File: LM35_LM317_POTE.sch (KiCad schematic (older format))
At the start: 21 parts, among them J10 TB_1X2, J6 TB_1X2, J7 TB_1X2, J8 TB_1X2, J9 TB_1X2, P10 CONN_01X02, P5 CONN_02X02, P6 CONN_01X02, P7 CONN_01X02, P8 CONN_01X02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

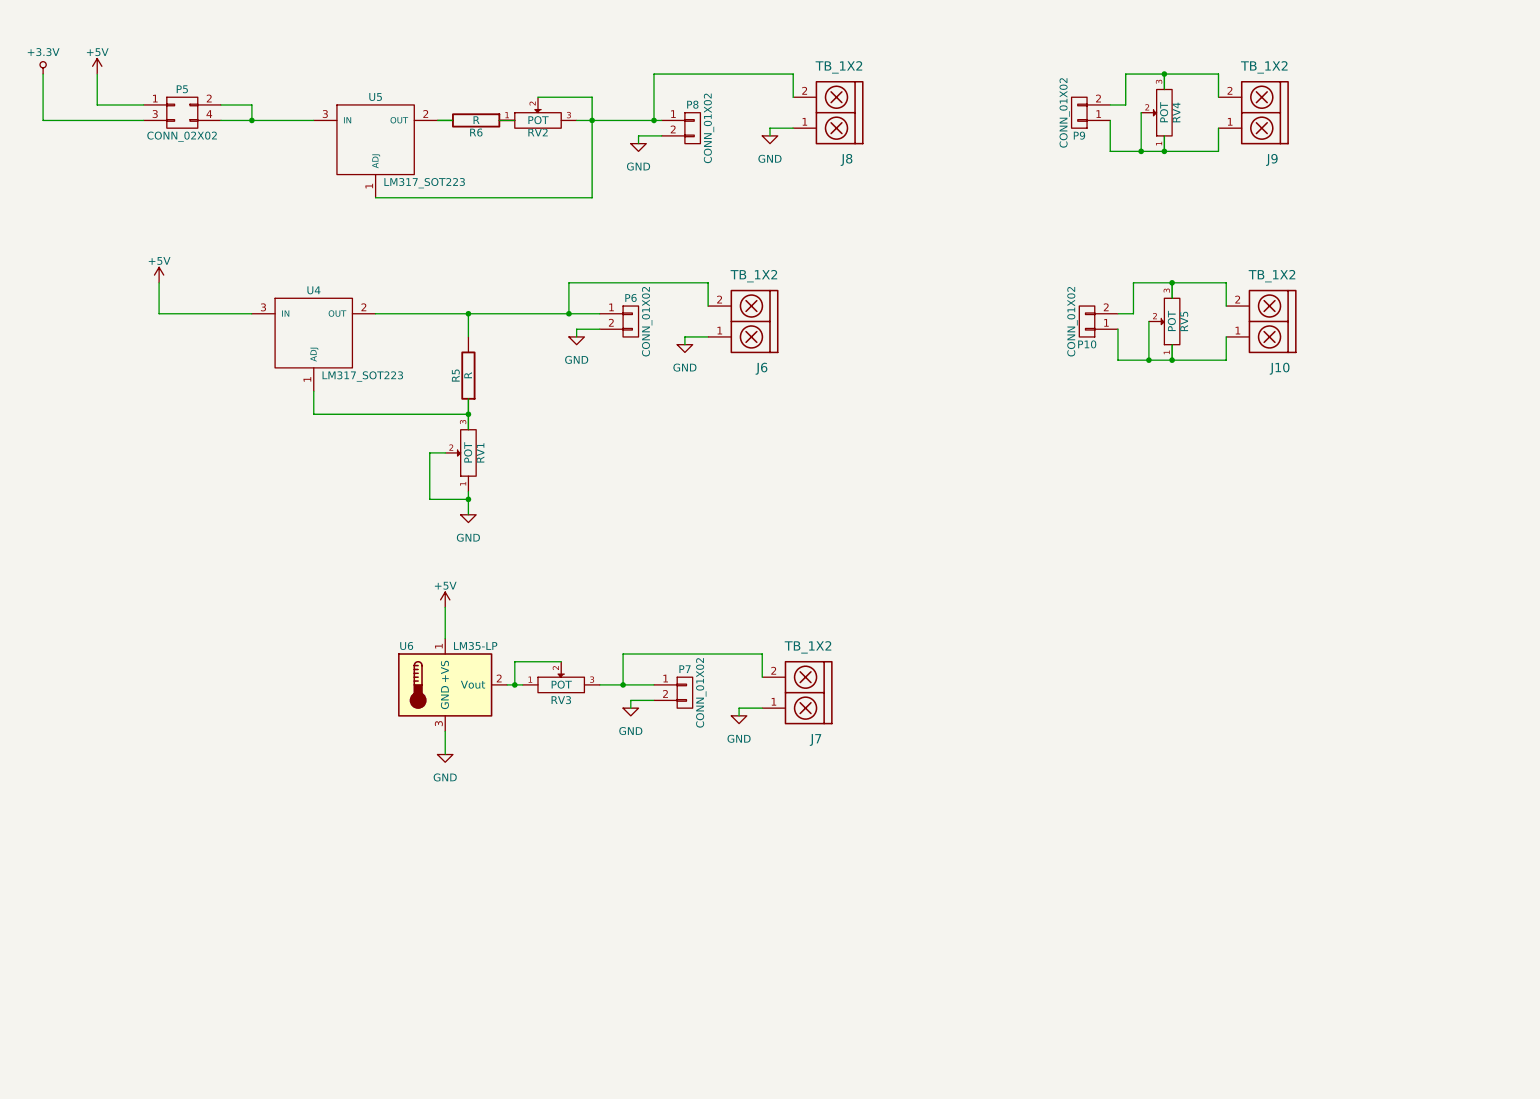
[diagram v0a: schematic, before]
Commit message: Modifico algunos componentes. Seteo algunos encapsulados. Ordeno los componentes en el PCB.
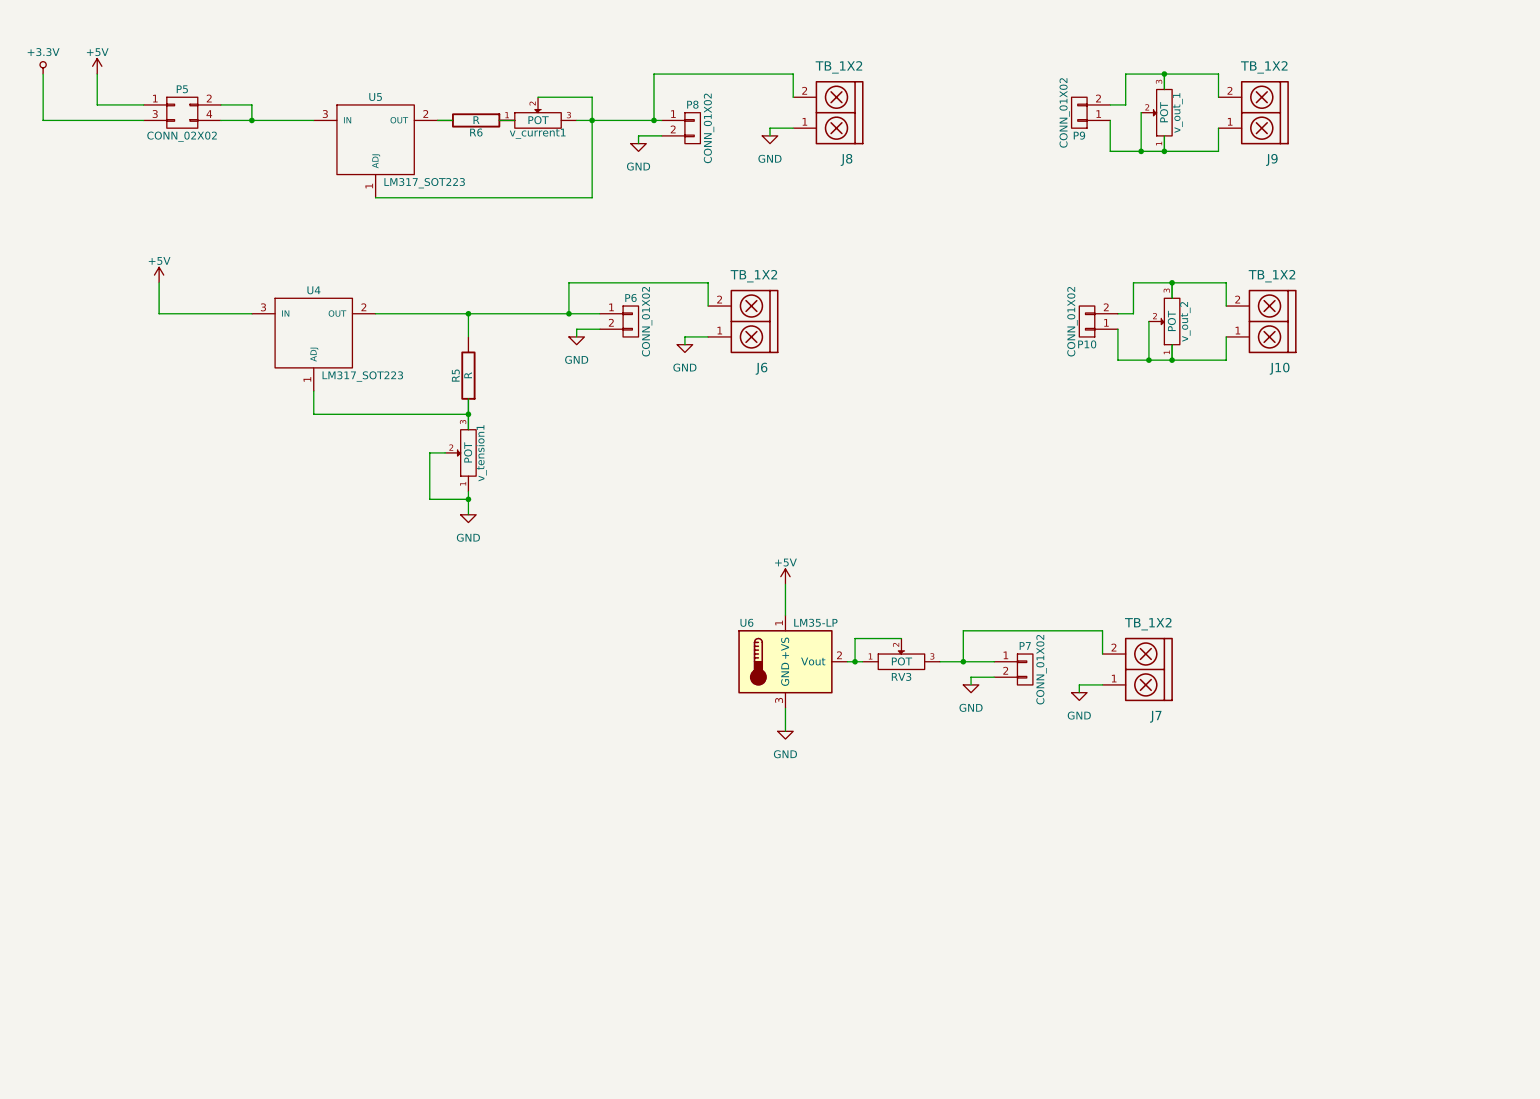
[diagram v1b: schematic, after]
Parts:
- J10, J6, J7, J8, J9: footprint (none) -> Connect:bornier2
- P10, P6, P7, P8, P9: footprint (none) -> Pin_Headers:Pin_Header_Angled_1x02
- P5: footprint (none) -> Pin_Headers:Pin_Header_Angled_2x02
- R5, R6: footprint (none) -> SMD_Packages:SMD-1206_Pol
- RV3: footprint (none) -> Potentiometers:Potentiometer_Alps-RK16-single
- U4, U5: footprint (none) -> TO_SOT_Packages_SMD:SOT-323
- U6: footprint (none) -> TO_SOT_Packages_THT:TO-92_Inline_Wide
- v_current1: renamed from RV2; footprint (none) -> Potentiometers:Potentiometer_Trimmer-Piher_PT15-V15_horizontal
- v_out_1: renamed from RV4; footprint (none) -> Potentiometers:Potentiometer_Alps-RK16-single_largePads
- v_out_2: renamed from RV5; footprint (none) -> Potentiometers:Potentiometer_Alps-RK16-single_largePads
- v_tension1: renamed from RV1; footprint (none) -> Potentiometers:Potentiometer_Trimmer-Piher_PT15-V15_horizontal
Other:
- moved on the sheet: J7, P7, RV3, U6

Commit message: Algunas modificaciones en el circuito  oreno el pcb.
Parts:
- P10, P6, P7, P8, P9: footprint Pin_Headers:Pin_Header_Angled_1x02 -> Pin_Headers:Pin_Header_Straight_1x02
- P5: footprint Pin_Headers:Pin_Header_Angled_2x02 -> Pin_Headers:Pin_Header_Straight_2x02
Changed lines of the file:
@@
 LIBS:video
 LIBS:xilinx
+LIBS:sim800l
 EELAYER 25 0
 EELAYER END
@@
 $EndComp
 $Comp
-L GND #PWR030
+L GND #PWR025
 U 1 1 581A256F
 P 4800 1450
-F 0 "#PWR030" H 4800 1200 50  0001 C CNN
+F 0 "#PWR025" H 4800 1200 50  0001 C CNN
 F 1 "GND" H 4800 1300 50  0000 C CNN
 F 2 "" H 4800 1450 50  0000 C CNN
@@
 F 0 "P8" H 5150 1500 50  0000 C CNN
 F 1 "CONN_01X02" V 5250 1350 50  0000 C CNN
-F 2 "Pin_Headers:Pin_Header_Angled_1x02" H 5150 1350 50  0001 C CNN
+F 2 "Pin_Headers:Pin_Header_Straight_1x02" H 5150 1350 50  0001 C CNN
 F 3 "" H 5150 1350 50  0000 C CNN
 	1    5150 1350
@@
 F 0 "P5" H 1850 1400 50  0000 C CNN
 F 1 "CONN_02X02" H 1850 1100 50  0000 C CNN
-F 2 "Pin_Headers:Pin_Header_Angled_2x02" H 1850 50  50  0001 C CNN
+F 2 "Pin_Headers:Pin_Header_Straight_2x02" H 1850 50  50  0001 C CNN
 F 3 "" H 1850 50  50  0000 C CNN
 	1    1850 1250
@@
 Connection ~ 2300 1300
 $Comp
-L +5V #PWR031
+L +5V #PWR026
 U 1 1 581A2572
 P 1300 1000
-F 0 "#PWR031" H 1300 850 50  0001 C CNN
+F 0 "#PWR026" H 1300 850 50  0001 C CNN
 F 1 "+5V" H 1300 1140 50  0000 C CNN
 F 2 "" H 1300 1000 50  0000 C CNN
@@
 	1300 1200 1300 1000
 $Comp
-L +3.3V-RESCUE-ciaa-nxp #PWR032
+L +3.3V-RESCUE-ciaa-nxp #PWR027
 U 1 1 581A2573
 P 950 1000
-F 0 "#PWR032" H 950 850 50  0001 C CNN
+F 0 "#PWR027" H 950 850 50  0001 C CNN
 F 1 "+3.3V" H 950 1140 50  0000 C CNN
 F 2 "" H 950 1000 50  0000 C CNN
@@
 $EndComp
 $Comp
-L GND #PWR033
+L GND #PWR028
 U 1 1 581A2577
 P 4400 2700
-F 0 "#PWR033" H 4400 2450 50  0001 C CNN
+F 0 "#PWR028" H 4400 2450 50  0001 C CNN
 F 1 "GND" H 4400 2550 50  0000 C CNN
 F 2 "" H 4400 2700 50  0000 C CNN
@@
 F 0 "P6" H 4750 2750 50  0000 C CNN
 F 1 "CONN_01X02" V 4850 2600 50  0000 C CNN
-F 2 "Pin_Headers:Pin_Header_Angled_1x02" H 4750 2600 50  0001 C CNN
+F 2 "Pin_Headers:Pin_Header_Straight_1x02" H 4750 2600 50  0001 C CNN
 F 3 "" H 4750 2600 50  0000 C CNN
 	1    4750 2600
@@
 $EndComp
 $Comp
-L +5V #PWR034
+L +5V #PWR029
 U 1 1 581A2579
 P 1700 2350
-F 0 "#PWR034" H 1700 2200 50  0001 C CNN
+F 0 "#PWR029" H 1700 2200 50  0001 C CNN
 F 1 "+5V" H 1700 2490 50  0000 C CNN
 F 2 "" H 1700 2350 50  0000 C CNN
@@
 Connection ~ 3700 2550
 $Comp
-L GND #PWR035
+L GND #PWR030
 U 1 1 581A257B
 P 3700 3850
-F 0 "#PWR035" H 3700 3600 50  0001 C CNN
+F 0 "#PWR030" H 3700 3600 50  0001 C CNN
 F 1 "GND" H 3700 3700 50  0000 C CNN
 F 2 "" H 3700 3850 50  0000 C CNN
@@
 Connection ~ 4350 2550
 $Comp
-L GND #PWR036
+L GND #PWR031
 U 1 1 581A257D
 P 5100 2750
-F 0 "#PWR036" H 5100 2500 50  0001 C CNN
+F 0 "#PWR031" H 5100 2500 50  0001 C CNN
 F 1 "GND" H 5100 2600 50  0000 C CNN
 F 2 "" H 5100 2750 50  0000 C CNN
@@
 	5800 1000 5800 1150
 $Comp
-L GND #PWR037
+L GND #PWR032
 U 1 1 581A257F
 P 5650 1400
-F 0 "#PWR037" H 5650 1150 50  0001 C CNN
+F 0 "#PWR032" H 5650 1150 50  0001 C CNN
 F 1 "GND" H 5650 1250 50  0000 C CNN
 F 2 "" H 5650 1400 50  0000 C CNN
@@
 F 0 "P9" H 7650 1400 50  0000 C CNN
 F 1 "CONN_01X02" V 7750 1250 50  0000 C CNN
-F 2 "Pin_Headers:Pin_Header_Angled_1x02" H 7650 1250 50  0001 C CNN
+F 2 "Pin_Headers:Pin_Header_Straight_1x02" H 7650 1250 50  0001 C CNN
 F 3 "" H 7650 1250 50  0000 C CNN
 	1    7650 1250
@@
 F 0 "P10" H 7700 2750 50  0000 C CNN
 F 1 "CONN_01X02" V 7800 2600 50  0000 C CNN
-F 2 "Pin_Headers:Pin_Header_Angled_1x02" H 7700 2600 50  0001 C CNN
+F 2 "Pin_Headers:Pin_Header_Straight_1x02" H 7700 2600 50  0001 C CNN
 F 3 "" H 7700 2600 50  0000 C CNN
 	1    7700 2600
@@
 $EndComp
 $Comp
-L +5V #PWR038
+L +5V #PWR033
 U 1 1 581A2587
 P 5750 4300
-F 0 "#PWR038" H 5750 4150 50  0001 C CNN
+F 0 "#PWR033" H 5750 4150 50  0001 C CNN
 F 1 "+5V" H 5750 4440 50  0000 C CNN
 F 2 "" H 5750 4300 50  0000 C CNN
@@
 Connection ~ 6200 4800
 $Comp
-L GND #PWR039
+L GND #PWR034
 U 1 1 581A2589
 P 6950 4950
-F 0 "#PWR039" H 6950 4700 50  0001 C CNN
+F 0 "#PWR034" H 6950 4700 50  0001 C CNN
 F 1 "GND" H 6950 4800 50  0000 C CNN
 F 2 "" H 6950 4950 50  0000 C CNN
@@
 F 0 "P7" H 7300 5000 50  0000 C CNN
 F 1 "CONN_01X02" V 7400 4850 50  0000 C CNN
-F 2 "Pin_Headers:Pin_Header_Angled_1x02" H 7300 4850 50  0001 C CNN
+F 2 "Pin_Headers:Pin_Header_Straight_1x02" H 7300 4850 50  0001 C CNN
 F 3 "" H 7300 4850 50  0000 C CNN
 	1    7300 4850
@@
 Connection ~ 6900 4800
 $Comp
-L GND #PWR040
+L GND #PWR035
 U 1 1 581A258C
 P 7650 5000
-F 0 "#PWR040" H 7650 4750 50  0001 C CNN
+F 0 "#PWR035" H 7650 4750 50  0001 C CNN
 F 1 "GND" H 7650 4850 50  0000 C CNN
 F 2 "" H 7650 5000 50  0000 C CNN
@@
 	6750 4800 7100 4800
 $Comp
-L GND #PWR041
+L GND #PWR036
 U 1 1 581A258D
 P 5750 5250
-F 0 "#PWR041" H 5750 5000 50  0001 C CNN
+F 0 "#PWR036" H 5750 5000 50  0001 C CNN
 F 1 "GND" H 5750 5100 50  0000 C CNN
 F 2 "" H 5750 5250 50  0000 C CNN

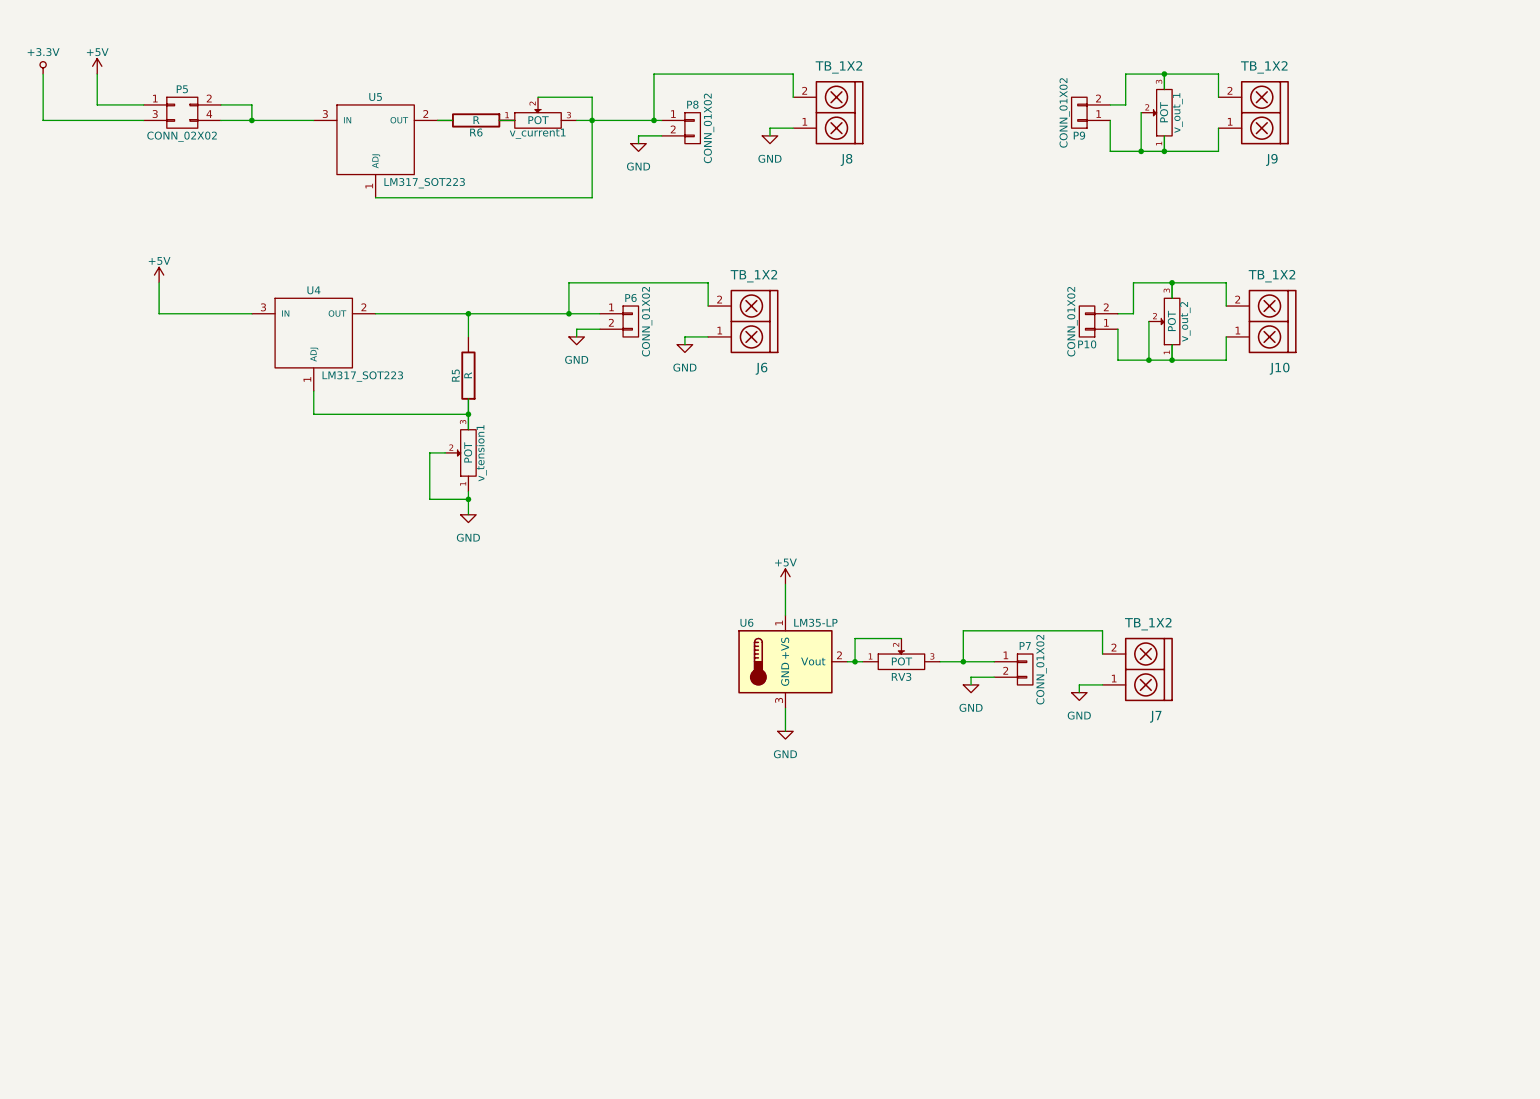
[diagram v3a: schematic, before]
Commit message: Modificaciones en el schematic dado los componentes comprados empiezo a ordenar los componentes en una dimension estimada de 10x6 cm.
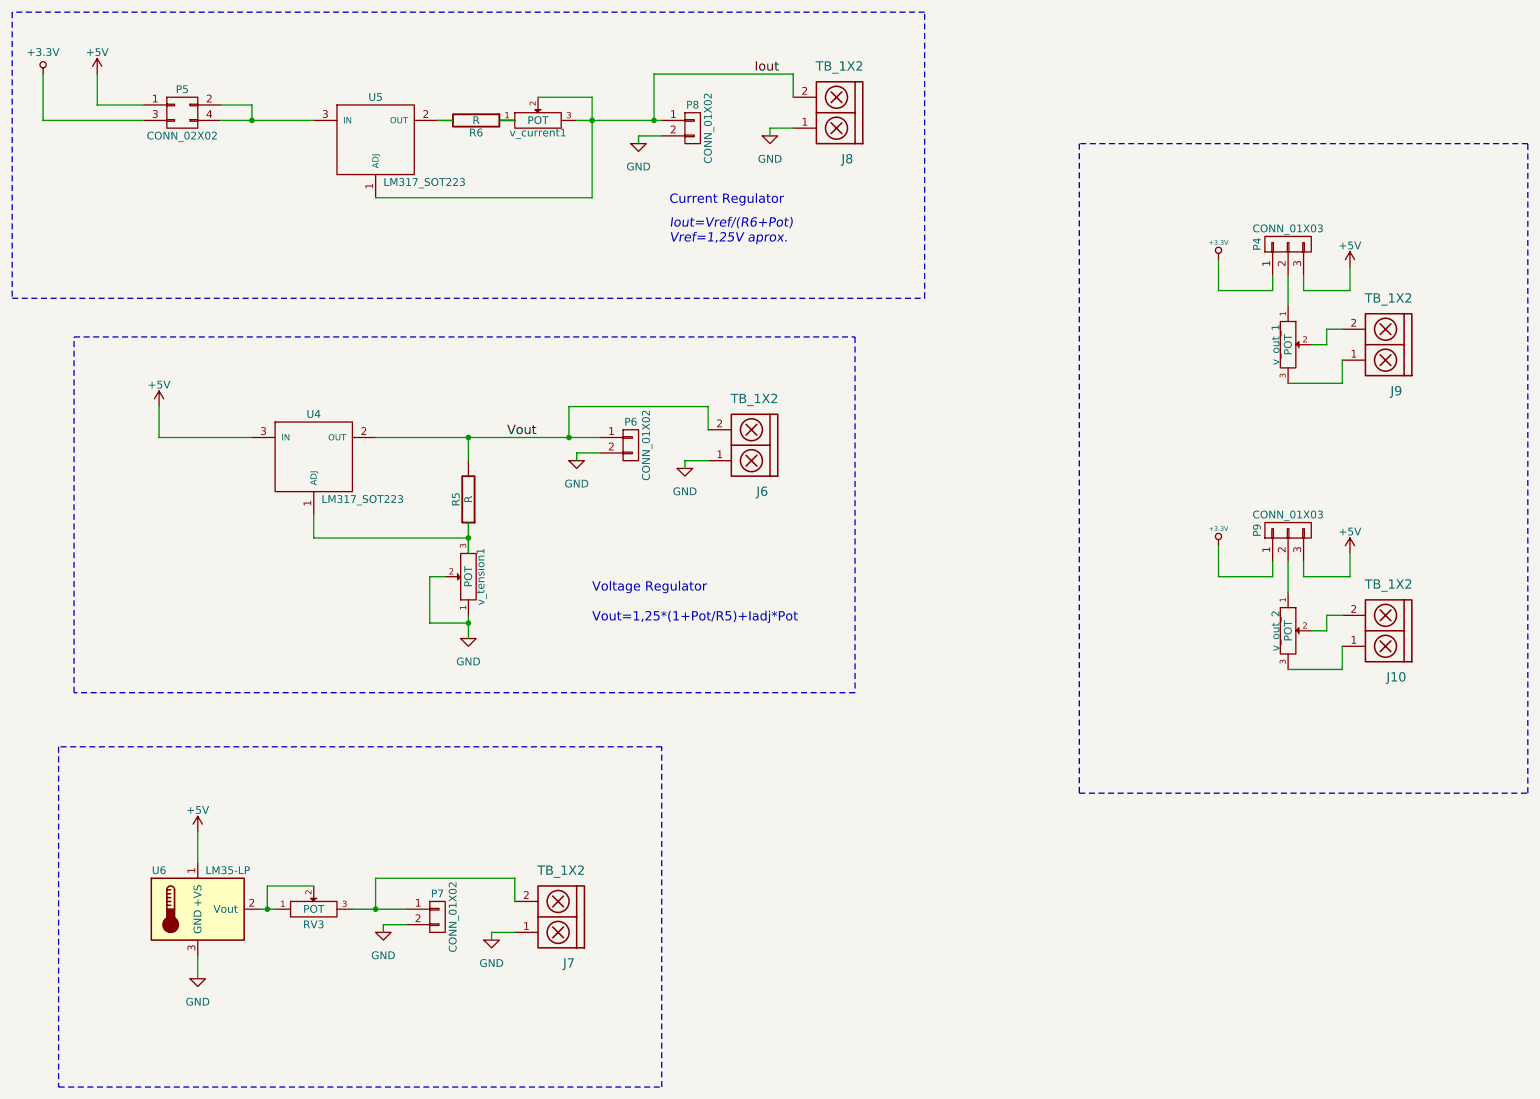
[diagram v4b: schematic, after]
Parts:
- removed P10, P9: CONN_01X02, Pin_Headers:Pin_Header_Straight_1x02, symbol CONN_01X02
- added P4, P9: CONN_01X03, Pin_Headers:Pin_Header_Straight_1x03, symbol CONN_01X03
- J10, J6, J7, J8, J9: footprint Connect:bornier2 -> Connect:AK300-2
- U4, U5: footprint TO_SOT_Packages_SMD:SOT-323 -> TO_SOT_Packages_THT:TO-220_Neutral123_Horizontal
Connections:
- net labels added: Iout, Vout
- wire segments 71 -> 75
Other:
- note added: "Current Regulator"
- note added: "Iout=Vref/(R6+Pot)\nVref=1,25V aprox."
- note added: "Voltage Regulator\n\nVout=1,25*(1+Pot/R5)+Iadj*Pot"
- moved on the sheet: J10, J6, J7, P6, P7, R5, RV3, U4, U6, v_out_2, v_tension1

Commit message: Modificaciones en el schematico.Cambio dimension a 10x7 cm.
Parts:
- U4, U5: footprint TO_SOT_Packages_THT:TO-220_Neutral123_Horizontal -> TO_SOT_Packages_THT:TO-220_Neutral123_Vertical
- v_current1, v_tension1: footprint Potentiometers:Potentiometer_Trimmer-Piher_PT15-V15_horizontal -> Potentiometers:Potentiometer_Bourns_3296W_3-8Zoll_Inline_ScrewUp
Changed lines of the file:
@@
 F 0 "v_current1" H 4150 1220 50  0000 C CNN
 F 1 "POT" H 4150 1300 50  0000 C CNN
-F 2 "Potentiometers:Potentiometer_Trimmer-Piher_PT15-V15_horizontal" H 4150 1300 50  0001 C CNN
+F 2 "Potentiometers:Potentiometer_Bourns_3296W_3-8Zoll_Inline_ScrewUp" H 4150 1300 50  0001 C CNN
 F 3 "" H 4150 1300 50  0000 C CNN
 	1    4150 1300
@@
 F 0 "U5" H 3100 1750 50  0000 C CNN
 F 1 "LM317_SOT223" H 3150 1200 50  0000 L CNN
-F 2 "TO_SOT_Packages_THT:TO-220_Neutral123_Horizontal" H 3100 1450 50  0001 C CNN
+F 2 "TO_SOT_Packages_THT:TO-220_Neutral123_Vertical" H 3100 1450 50  0001 C CNN
 F 3 "" H 3100 1450 50  0000 C CNN
 	1    3100 1450
@@
 F 0 "v_tension1" H 3700 4170 50  0000 C CNN
 F 1 "POT" H 3700 4250 50  0000 C CNN
-F 2 "Potentiometers:Potentiometer_Trimmer-Piher_PT15-V15_horizontal" H 3700 4250 50  0001 C CNN
+F 2 "Potentiometers:Potentiometer_Bourns_3296W_3-8Zoll_Inline_ScrewUp" H 3700 4250 50  0001 C CNN
 F 3 "" H 3700 4250 50  0000 C CNN
 	1    3700 4250
@@
 F 0 "U4" H 2700 3800 50  0000 C CNN
 F 1 "LM317_SOT223" H 2750 3250 50  0000 L CNN
-F 2 "TO_SOT_Packages_THT:TO-220_Neutral123_Horizontal" H 2700 3500 50  0001 C CNN
+F 2 "TO_SOT_Packages_THT:TO-220_Neutral123_Vertical" H 2700 3500 50  0001 C CNN
 F 3 "" H 2700 3500 50  0000 C CNN
 	1    2700 3500
